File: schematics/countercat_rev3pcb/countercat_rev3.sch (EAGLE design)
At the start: 59 parts, among them Q1 IRF520, Q3 IRF520, Q4 IRF520, Q5 IRF520, U4 ATMEGA328P, Y1 16MHz

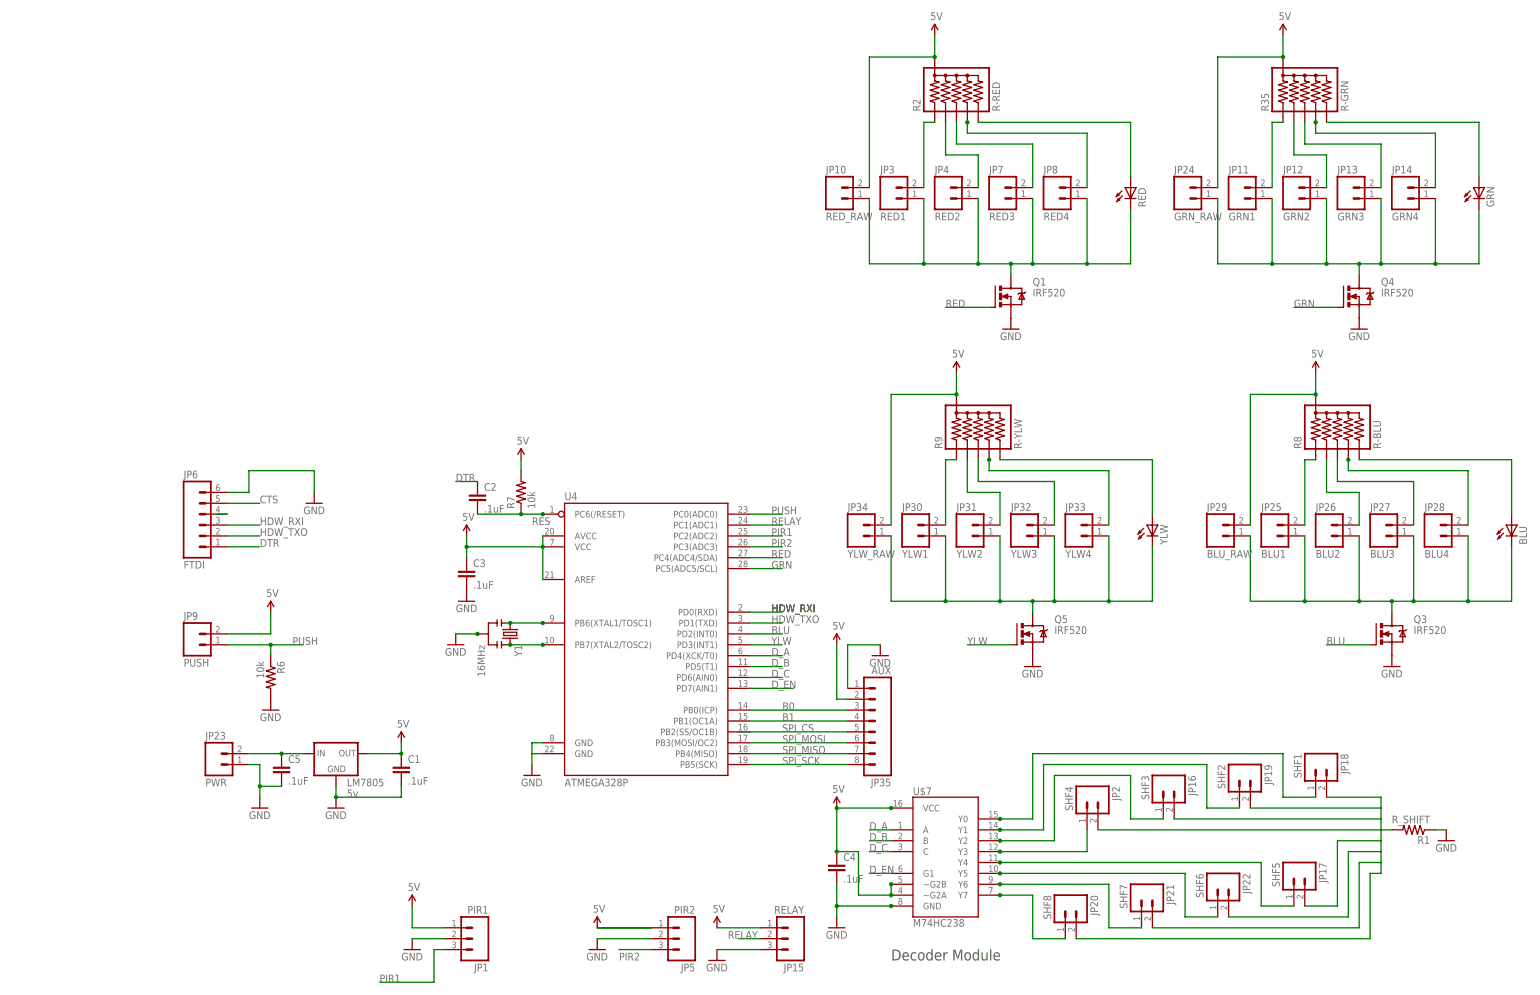
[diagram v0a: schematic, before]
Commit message: Added PDF of board schematic
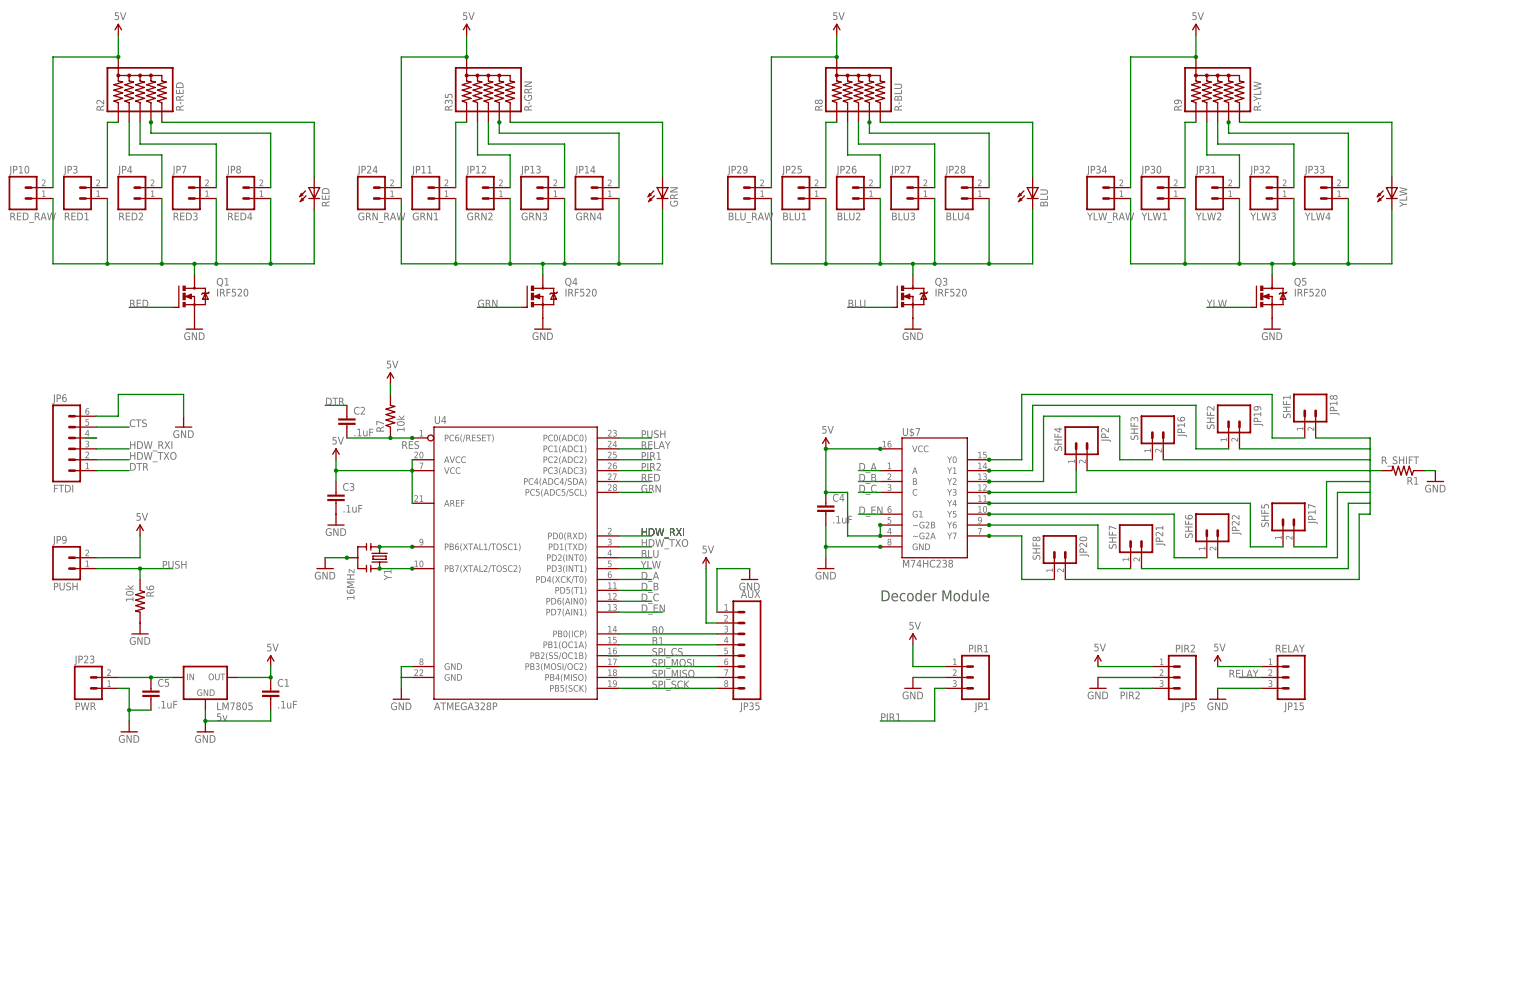
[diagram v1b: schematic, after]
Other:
- moved on the sheet: BLU, C1, C2, C3, C4, C5, GRN, JP1, JP10, JP11, JP12, JP13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
